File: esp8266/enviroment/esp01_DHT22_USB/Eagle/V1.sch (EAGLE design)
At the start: 13 parts, among them IC1 LD117AV33, X1 MINI-USB_4P-85-32004-10X

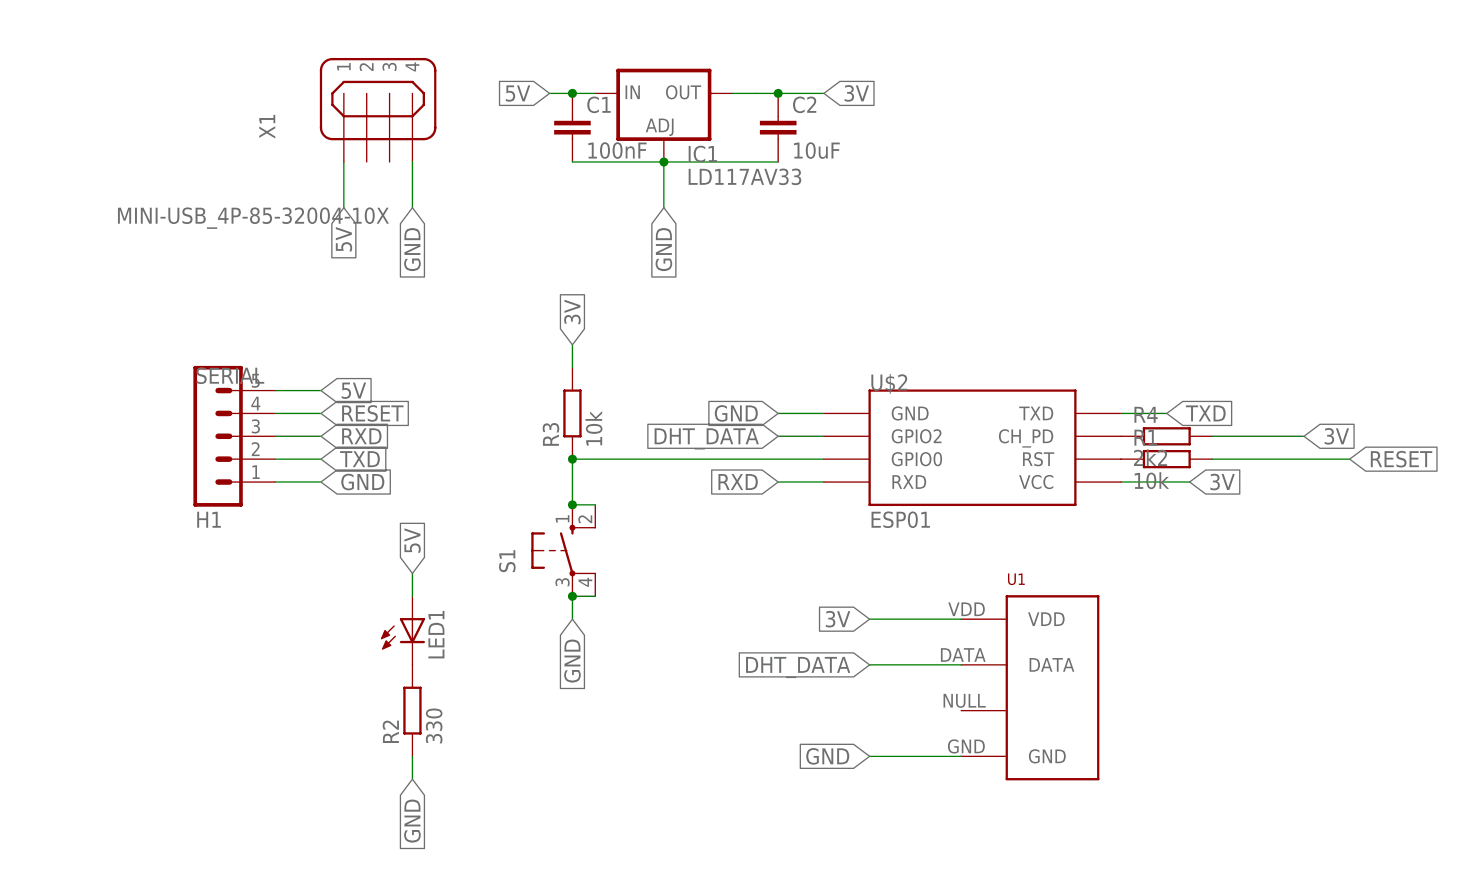
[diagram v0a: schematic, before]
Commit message: Changed Programmer-Pinout
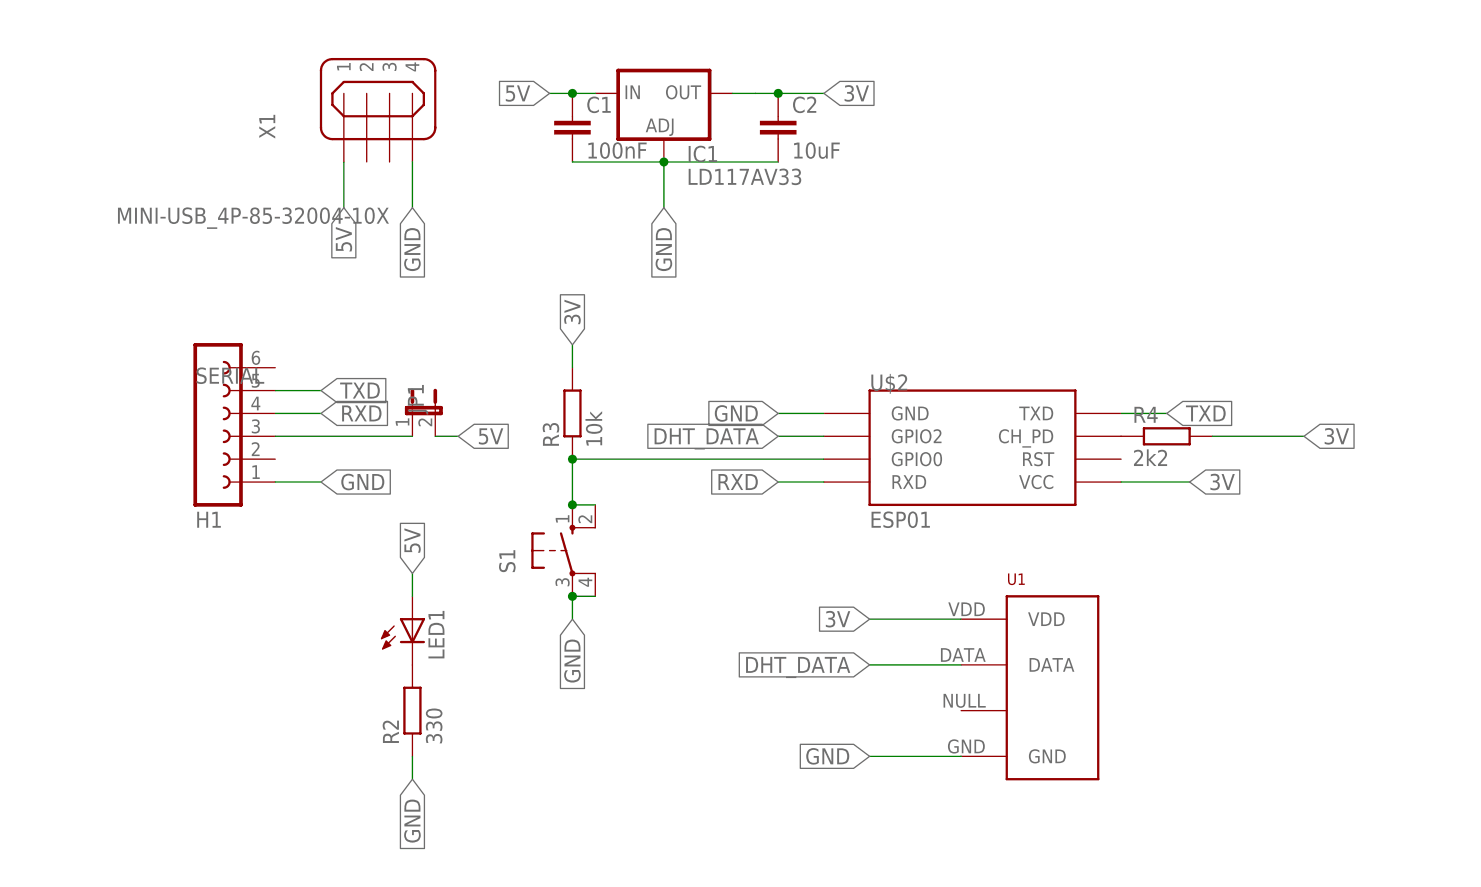
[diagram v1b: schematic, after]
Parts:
- removed R1: 10k, rcl:R-EU_0207/10
- added JP1: (no value), jumper:JP1E
- SERIAL: device con-lstb:MA05-1 -> con-lsta:FE06-1
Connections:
- removed net RESET: R1.2, SERIAL.4
- net 5V: now also JP1.2; no longer SERIAL.5
- net N$1: now also JP1.1, SERIAL.3; no longer R1.1, U$2.RST
- net RXD: now also SERIAL.4; no longer SERIAL.3
- net TXD: now also SERIAL.5; no longer SERIAL.2

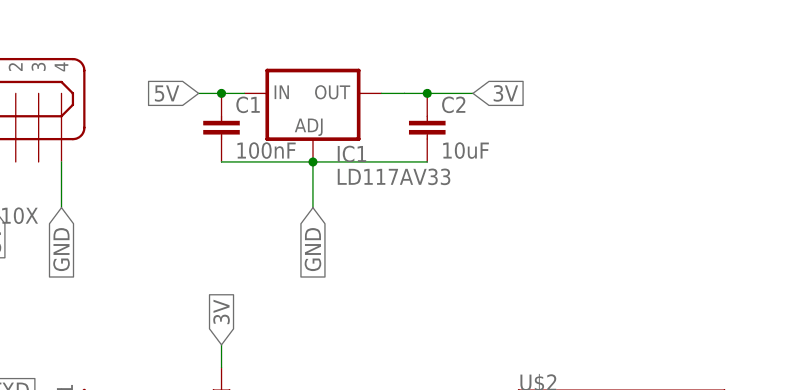
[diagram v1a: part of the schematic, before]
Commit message: Changed Voltage-Regulator to fit pseudo-standart pinout
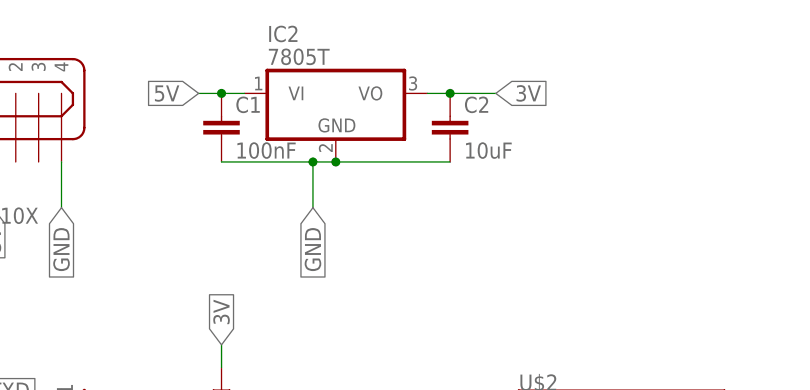
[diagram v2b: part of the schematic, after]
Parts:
- removed IC1: LD117AV33, v-reg:LD117AV33
- added IC2: 7805T, linear:7805T
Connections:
- net 3V: now also IC2.VO; no longer IC1.OUT
- net 5V: now also IC2.VI; no longer IC1.IN
- net GND: now also IC2.GND; no longer IC1.ADJ
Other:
- moved on the sheet: C2
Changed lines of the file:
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@@
 <?xml version="1.0" encoding="utf-8"?>
 <!DOCTYPE eagle SYSTEM "eagle.dtd">
-<eagle version="9.2.1">
+<eagle version="9.2.2">
 <drawing>
 <settings>
@@
 <part name="U$2" library="esp8266modules" deviceset="ESP01" device=""/>
 <part name="X1" library="con-cypressindustries" library_urn="urn:adsk.eagle:library:138" deviceset="MINI-USB_4P-" device="85-32004-10X" package3d_urn="urn:adsk.eagle:package:6445/1"/>
-<part name="IC1" library="v-reg" library_urn="urn:adsk.eagle:library:409" deviceset="LD117A?*" device="V" package3d_urn="urn:adsk.eagle:package:30365/1" technology="33"/>
 <part name="C1" library="rcl" library_urn="urn:adsk.eagle:library:334" deviceset="C-EU" device="025-030X050" package3d_urn="urn:adsk.eagle:package:23631/1" value="100nF"/>
 <part name="C2" library="rcl" library_urn="urn:adsk.eagle:library:334" deviceset="C-EU" device="025-030X050" package3d_urn="urn:adsk.eagle:package:23631/1" value="10uF"/>
@@
 <part name="R4" library="rcl" library_urn="urn:adsk.eagle:library:334" deviceset="R-EU_" device="0207/10" package3d_urn="urn:adsk.eagle:package:23491/1" value="2k2"/>
 <part name="JP1" library="jumper" library_urn="urn:adsk.eagle:library:252" deviceset="JP1E" device="" package3d_urn="urn:adsk.eagle:package:15455/1"/>
+<part name="IC2" library="linear" library_urn="urn:adsk.eagle:library:262" deviceset="78*" device="T" package3d_urn="urn:adsk.eagle:package:16414/1" technology="05"/>
 </parts>
 <sheets>
@@
 <attribute name="VALUE" x="-7.62" y="66.04" size="1.778" layer="96" rot="R180"/>
 </instance>
-<instance part="IC1" gate="G$1" x="22.86" y="78.74" smashed="yes">
-<attribute name="NAME" x="25.4" y="71.12" size="1.778" layer="95"/>
-<attribute name="VALUE" x="25.4" y="68.58" size="1.778" layer="96"/>
-</instance>
 <instance part="C1" gate="G$1" x="12.7" y="76.2" smashed="yes">
 <attribute name="NAME" x="14.224" y="76.581" size="1.778" layer="95"/>
 <attribute name="VALUE" x="14.224" y="71.501" size="1.778" layer="96"/>
 </instance>
-<instance part="C2" gate="G$1" x="35.56" y="76.2" smashed="yes">
-<attribute name="NAME" x="37.084" y="76.581" size="1.778" layer="95"/>
-<attribute name="VALUE" x="37.084" y="71.501" size="1.778" layer="96"/>
+<instance part="C2" gate="G$1" x="38.1" y="76.2" smashed="yes">
+<attribute name="NAME" x="39.624" y="76.581" size="1.778" layer="95"/>
+<attribute name="VALUE" x="39.624" y="71.501" size="1.778" layer="96"/>
 </instance>
 <instance part="SERIAL" gate="G$1" x="-27.94" y="40.64" smashed="yes">
@@
 <attribute name="NAME" x="-3.81" y="43.18" size="1.778" layer="95" rot="R90"/>
 <attribute name="VALUE" x="0.635" y="43.18" size="1.778" layer="96" rot="R90"/>
+</instance>
+<instance part="IC2" gate="A1" x="25.4" y="78.74" smashed="yes">
+<attribute name="NAME" x="17.78" y="84.455" size="1.778" layer="95"/>
+<attribute name="VALUE" x="17.78" y="81.915" size="1.778" layer="96"/>
 </instance>
 </instances>
@@
 <wire x1="22.86" y1="71.12" x2="22.86" y2="66.04" width="0.1524" layer="91"/>
 <label x="22.86" y="66.04" size="1.778" layer="95" rot="R270" xref="yes"/>
-<pinref part="IC1" gate="G$1" pin="ADJ"/>
 <pinref part="C1" gate="G$1" pin="2"/>
 <wire x1="12.7" y1="71.12" x2="22.86" y2="71.12" width="0.1524" layer="91"/>
 <junction x="22.86" y="71.12"/>
 <pinref part="C2" gate="G$1" pin="2"/>
-<wire x1="22.86" y1="71.12" x2="35.56" y2="71.12" width="0.1524" layer="91"/>
+<wire x1="22.86" y1="71.12" x2="25.4" y2="71.12" width="0.1524" layer="91"/>
+<pinref part="IC2" gate="A1" pin="GND"/>
+<wire x1="25.4" y1="71.12" x2="38.1" y2="71.12" width="0.1524" layer="91"/>
+<junction x="25.4" y="71.12"/>
 </segment>
 <segment>
@@
 <segment>
 <label x="10.16" y="78.74" size="1.778" layer="95" rot="R180" xref="yes"/>
-<pinref part="IC1" gate="G$1" pin="IN"/>
 <wire x1="15.24" y1="78.74" x2="12.7" y2="78.74" width="0.1524" layer="91"/>
 <pinref part="C1" gate="G$1" pin="1"/>
 <wire x1="12.7" y1="78.74" x2="10.16" y2="78.74" width="0.1524" layer="91"/>
 <junction x="12.7" y="78.74"/>
+<pinref part="IC2" gate="A1" pin="VI"/>
 </segment>
 <segment>
@@
 <net name="3V" class="0">
 <segment>
-<wire x1="33.02" y1="78.74" x2="35.56" y2="78.74" width="0.1524" layer="91"/>
-<label x="40.64" y="78.74" size="1.778" layer="95" xref="yes"/>
-<pinref part="IC1" gate="G$1" pin="OUT"/>
-<wire x1="35.56" y1="78.74" x2="40.64" y2="78.74" width="0.1524" layer="91"/>
-<wire x1="30.48" y1="78.74" x2="33.02" y2="78.74" width="0.1524" layer="91"/>
+<label x="43.18" y="78.74" size="1.778" layer="95" xref="yes"/>
 <pinref part="C2" gate="G$1" pin="1"/>
-<junction x="35.56" y="78.74"/>
-</segment>
-<segment>
+<pinref part="IC2" gate="A1" pin="VO"/>
+<wire x1="38.1" y1="78.74" x2="35.56" y2="78.74" width="0.1524" layer="91"/>
+<wire x1="38.1" y1="78.74" x2="43.18" y2="78.74" width="0.1524" layer="91"/>
+<junction x="38.1" y="78.74"/>
+</segment>
+<segment>
